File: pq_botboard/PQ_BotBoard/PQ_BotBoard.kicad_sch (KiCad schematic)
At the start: 28 parts, among them IC1 TCN75AVOA713, J1 53261-1471, J2 Conn_01x08_MountingPin, J3 53261-0271

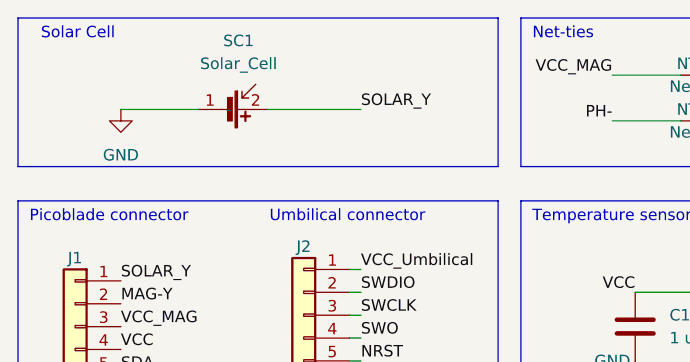
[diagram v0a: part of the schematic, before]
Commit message: Updated outer boards design as required by the change from Azur Space house-cut solar cells to Lighttricity's S3040_CIC model. Preserved the older design in lat_board_old
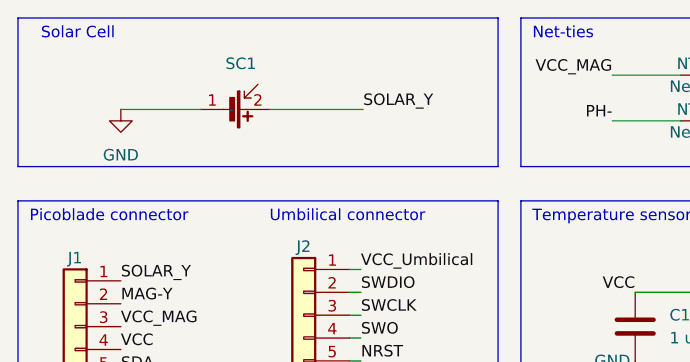
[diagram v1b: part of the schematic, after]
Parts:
- removed SC1: Solar_Cell, -nsl_power:Azur-Space-PQ-cut-SC, symbol power-nsl:Solar_Cell
- added SC1: ~, power-nsl:Lighttricity_S3040_CIC, symbol power-nsl:S3040_CIC
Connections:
- net GND: now also SC1.1 (-)
- net SOLAR_Y: now also SC1.2
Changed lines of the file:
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@@
     (stroke (width 0) (type default))
   )
-  (wire (pts (xy 87.63 52.07) (xy 96.266 52.07))
+  (wire (pts (xy 87.63 52.07) (xy 96.52 52.07))
     (stroke (width 0) (type default))
   )
@@
     (stroke (width 0) (type default))
   )
+  (wire (pts (xy 104.14 52.07) (xy 114.554 52.07))
+    (stroke (width 0) (type default))
+  )
   (wire (pts (xy 191.77 72.39) (xy 191.77 77.47))
     (stroke (width 0) (type default))
@@
   )
   (wire (pts (xy 114.3 85.09) (xy 113.03 85.09))
-    (stroke (width 0) (type default))
-  )
-  (wire (pts (xy 103.886 52.07) (xy 114.3 52.07))
     (stroke (width 0) (type default))
   )
@@
     (effects (font (size 1.27 1.27)) (justify right bottom))
   )
-  (label "SOLAR_Y" (at 114.3 52.07 0) (fields_autoplaced)
+  (label "SOLAR_Y" (at 114.554 52.07 0) (fields_autoplaced)
     (effects (font (size 1.27 1.27)) (justify left bottom))
   )
@@
         (path "/e40a5bef-c31a-474e-b379-53d1d13d8a60"
           (reference "#PWR0108") (unit 1)
+        )
+      )
+    )
+  )
+  (symbol (lib_id "power-nsl:S3040_CIC") (at 100.33 52.07 270) (unit 1)
+    (in_bom yes) (on_board yes) (dnp no) (fields_autoplaced)
+    (property "Reference" "SC1" (at 100.965 46.99 90)
+      (effects (font (size 1.27 1.27)))
+    )
+    (property "Value" "~" (at 100.33 52.07 0)
+      (effects (font (size 1.27 1.27)))
+    )
+    (property "Footprint" "power-nsl:Lighttricity_S3040_CIC" (at 100.33 52.07 0)
+      (effects (font (size 1.27 1.27)) hide)
+    )
+    (property "Datasheet" "" (at 100.33 52.07 0)
+      (effects (font (size 1.27 1.27)) hide)
+    )
+    (pin "1")
+    (pin "2")
+    (instances
+      (project "PQ_BotBoard"
+        (path "/e40a5bef-c31a-474e-b379-53d1d13d8a60"
+          (reference "SC1") (unit 1)
         )
       )
@@
         )
       )
-    )
-  )
-  (symbol (lib_id "power-nsl:Solar_Cell") (at 100.33 52.07 270) (unit 1)
-    (in_bom yes) (on_board yes) (dnp no) (fields_autoplaced)
-    (property "Reference" "SC1" (at 100.711 44.45 90)
-      (effects (font (size 1.27 1.27)))
-    )
-    (property "Value" "Solar_Cell" (at 100.711 46.99 90)
-      (effects (font (size 1.27 1.27)))
-    )
-    (property "Footprint" "-nsl_power:Azur-Space-PQ-cut-SC" (at 98.806 62.484 0)
-      (effects (font (size 1.27 1.27)) hide)
-    )
-    (property "Datasheet" "" (at 98.806 62.484 0)
-      (effects (font (size 1.27 1.27)) hide)
-    )
-    (property "Manufacturer 1" "Azur Space" (at 100.33 52.07 0)
-      (effects (font (size 1.27 1.27)) hide)
-    )
-    (property "Manufacturer Part Number 1" "3G30A" (at 100.33 52.07 0)
-      (effects (font (size 1.27 1.27)) hide)
-    )
-    (property "Supplier 1" "Lighttricity" (at 100.33 52.07 0)
-      (effects (font (size 1.27 1.27)) hide)
-    )
-    (property "Supplier Part Number 1" "N/A" (at 100.33 52.07 0)
-      (effects (font (size 1.27 1.27)) hide)
-    )
-    (pin "1")
-    (pin "2")
-    (instances
-      (project "PQ_BotBoard"
-        (path "/e40a5bef-c31a-474e-b379-53d1d13d8a60"
-          (reference "SC1") (unit 1)
-        )
-      )

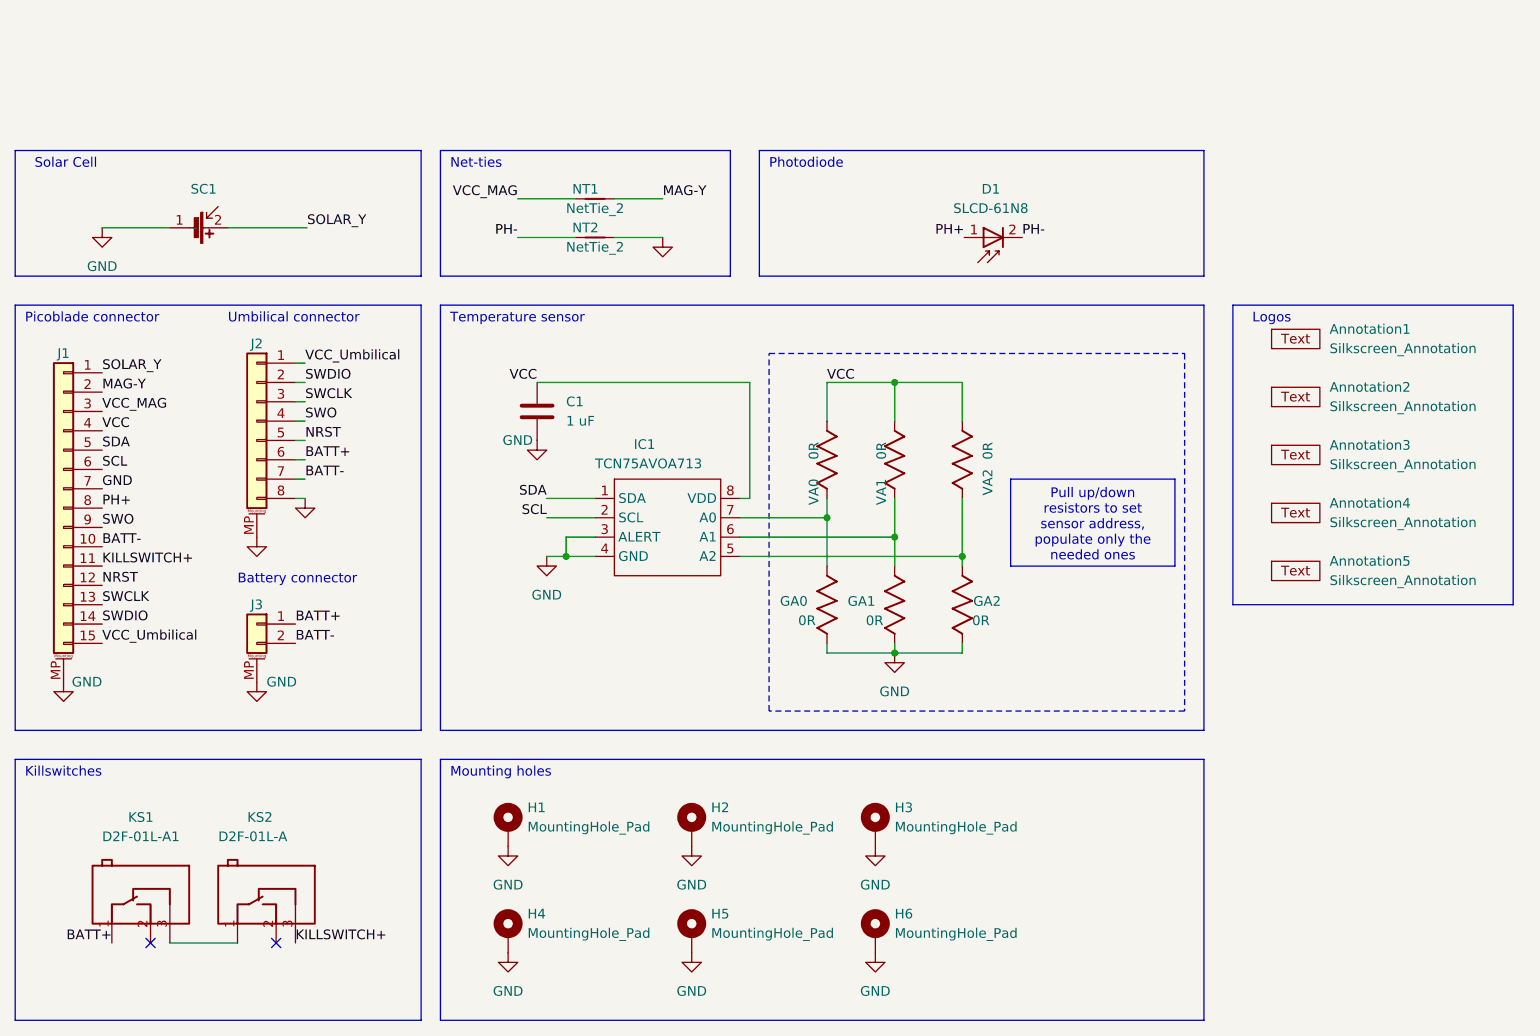
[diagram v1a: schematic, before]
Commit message: fix mirroring of Lightricity's solar cells
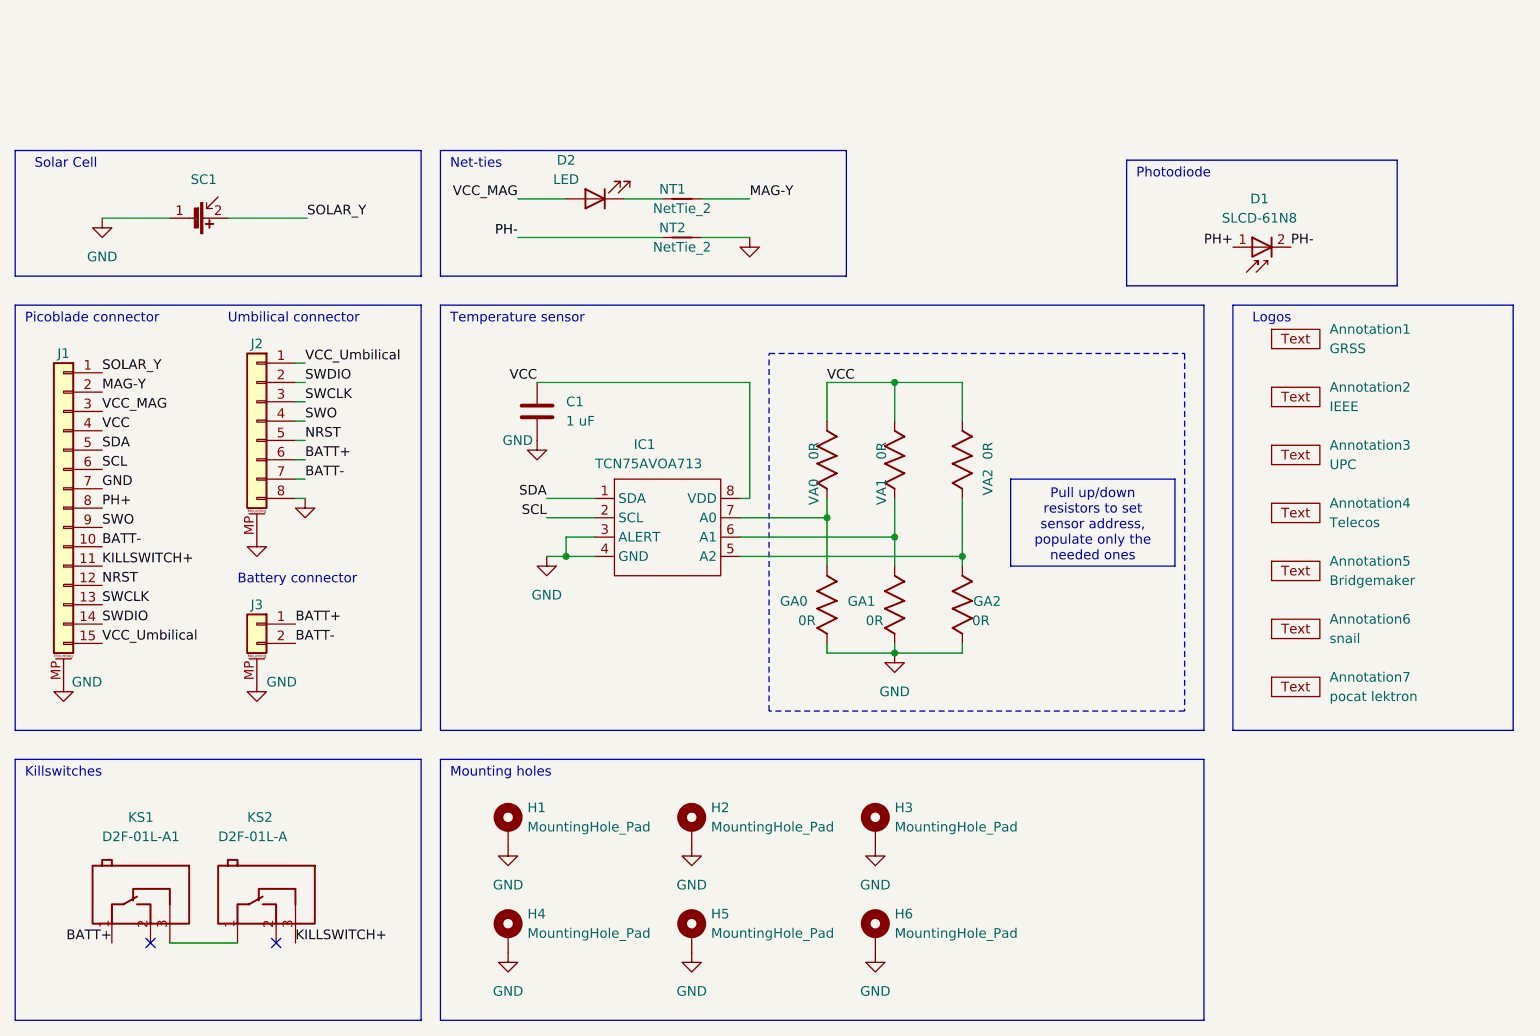
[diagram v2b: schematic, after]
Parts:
- added Annotation6: snail, symbols-nsl:snail, symbol symbols-nsl:Silkscreen_Annotation
- added Annotation7: pocat lektron, symbols-nsl:pocat-lektron, symbol symbols-nsl:Silkscreen_Annotation
- added D2: LED, LED_SMD:LED_0402_1005Metric, symbol Device:LED
- Annotation1: value Silkscreen_Annotation -> GRSS
- Annotation2: value Silkscreen_Annotation -> IEEE
- Annotation3: value Silkscreen_Annotation -> UPC
- Annotation4: value Silkscreen_Annotation -> Telecos
- Annotation5: value Silkscreen_Annotation -> Bridgemaker
- SC1: footprint power-nsl:Lighttricity_S3040_CIC -> power-nsl:Lighttricity_S3040_CIC_
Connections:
- net VCC_MAG: now also D2.2 (A); no longer NT1.1
- new net: D2.1 (K), NT1.1
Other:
- moved on the sheet: D1, NT1, NT2, SC1

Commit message: Removed netie, updated SC footprint, trace reform, logo&name cleanup, footprint reconciled, DRC, centered umbilical connector
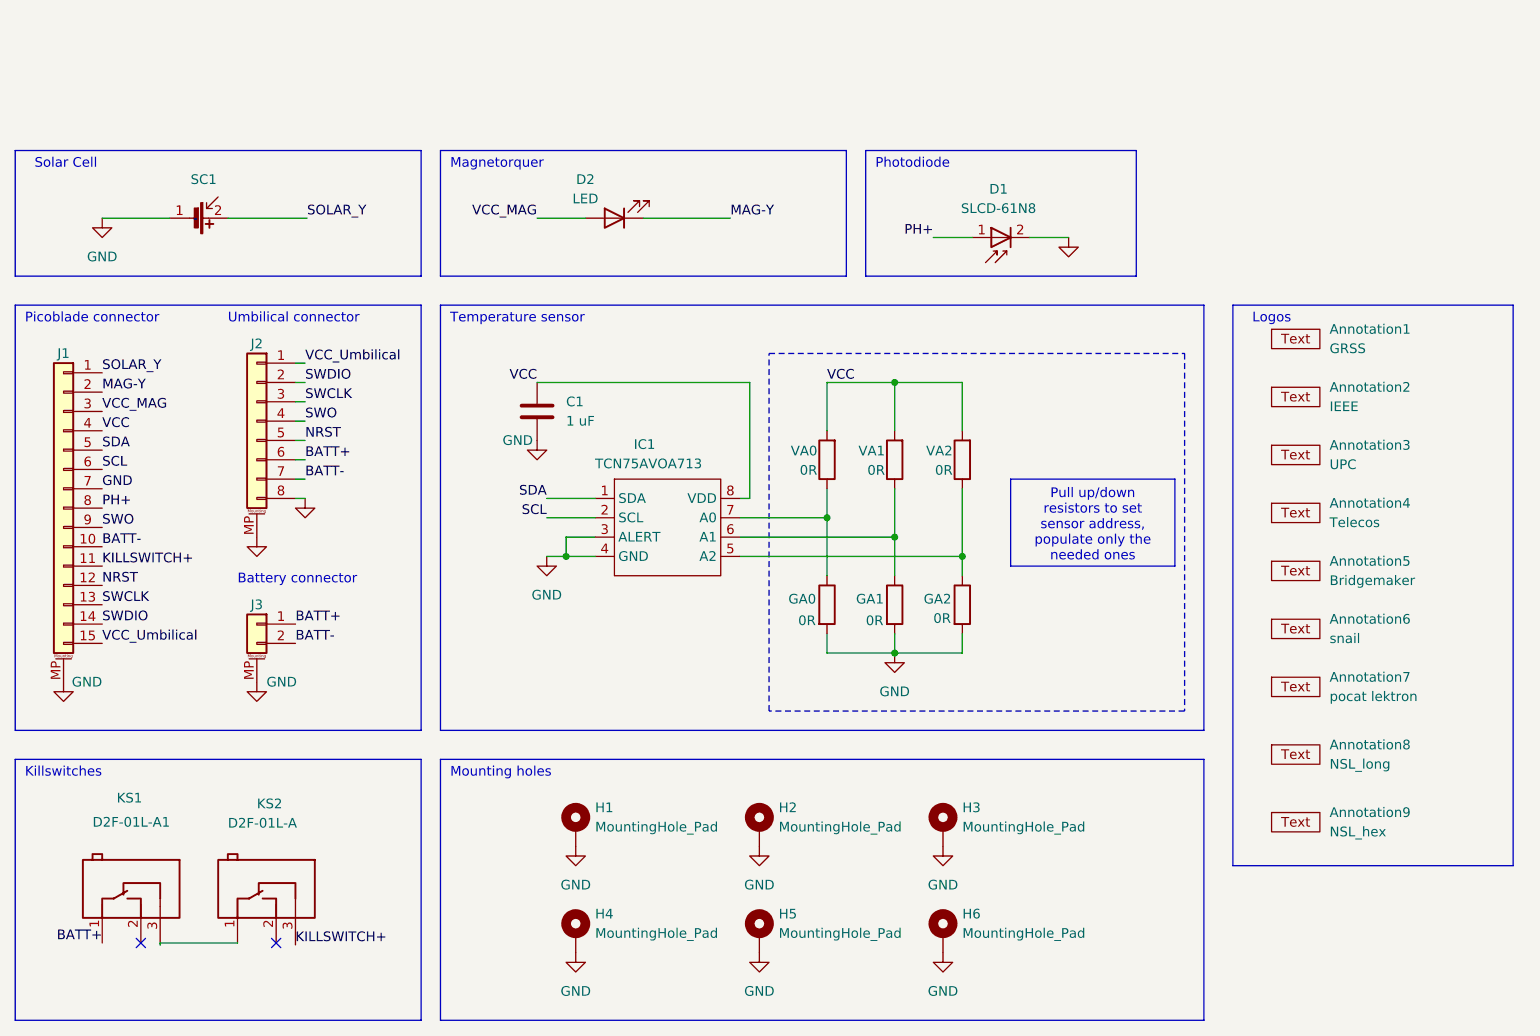
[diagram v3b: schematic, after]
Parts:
- removed NT1, NT2: NetTie_2, NetTie:NetTie-2_SMD_Pad0.5mm, symbol Device:NetTie_2
- added Annotation8: NSL_long, symbols-nsl:NSL-small, symbol symbols-nsl:Silkscreen_Annotation
- added Annotation9: NSL_hex, symbols-nsl:NSL_hexagon, symbol symbols-nsl:Silkscreen_Annotation
- Annotation1: footprint -nsl_symbols:GRSS -> symbols-nsl:GRSS
- Annotation2: footprint -nsl_symbols:IEEE_logo -> symbols-nsl:IEEE_logo
- Annotation3: footprint -nsl_symbols:UPC_positiu -> symbols-nsl:UPC_positiu
- Annotation4: footprint -nsl_symbols:Telecos -> symbols-nsl:Telecos
- Annotation5: footprint -nsl_symbols:Bridgemaker -> symbols-nsl:Bridgemaker
- Annotation6: footprint symbols-nsl:snail -> symbols-nsl:Snail
- D1: footprint -nsl_passive:SLCD-61N8 -> passive-nsl:SLCD-61N8
- GA0, GA1, GA2: symbol Lateral_board-altium-import:1_5k -> Device:R
- IC1: footprint -nsl_sensor:TCN75AVOA -> sensor-nsl:TCN75AVOA
- KS1: footprint -nsl_miscellaneous:D2FLA1 -> miscelaneous-nsl:D2FLA1; symbol Bottom_board-altium-import:0_D2F-01L-A -> miscelaneous-nsl:D2FLA
- KS2: footprint -nsl_miscellaneous:D2FLA -> miscelaneous-nsl:D2FLA; symbol Bottom_board-altium-import:0_D2F-01L-A1 -> miscelaneous-nsl:D2FLA
- SC1: footprint power-nsl:Lighttricity_S3040_CIC_ -> power-nsl:Lighttricity_S3040_CIC
- VA0, VA1, VA2: symbol Lateral_board-altium-import:0_5k -> Device:R
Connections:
- net PH- is gone; now on net GND: D1.2
- net GND: now also GA0.2, GA1.2, GA2.2; no longer GA0.1, GA1.1, GA2.1
- net MAG-Y: now also D2.1 (K)
- net at IC1.7 (A0), VA0.1: now also GA0.1; no longer GA0.2
- net at IC1.5 (A2), VA2.1: now also GA2.1; no longer GA2.2
- net at IC1.6 (A1), VA1.1: now also GA1.1; no longer GA1.2
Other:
- note added: "Magnetorquer"
- note removed: "Net-ties"
- moved on the sheet: D1, D2, H1, H2, H3, H4, H5, H6

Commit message: Added a charging protection for the battery using the umbilical (antireturn Schottky diode and LDO) and regenerated the production files
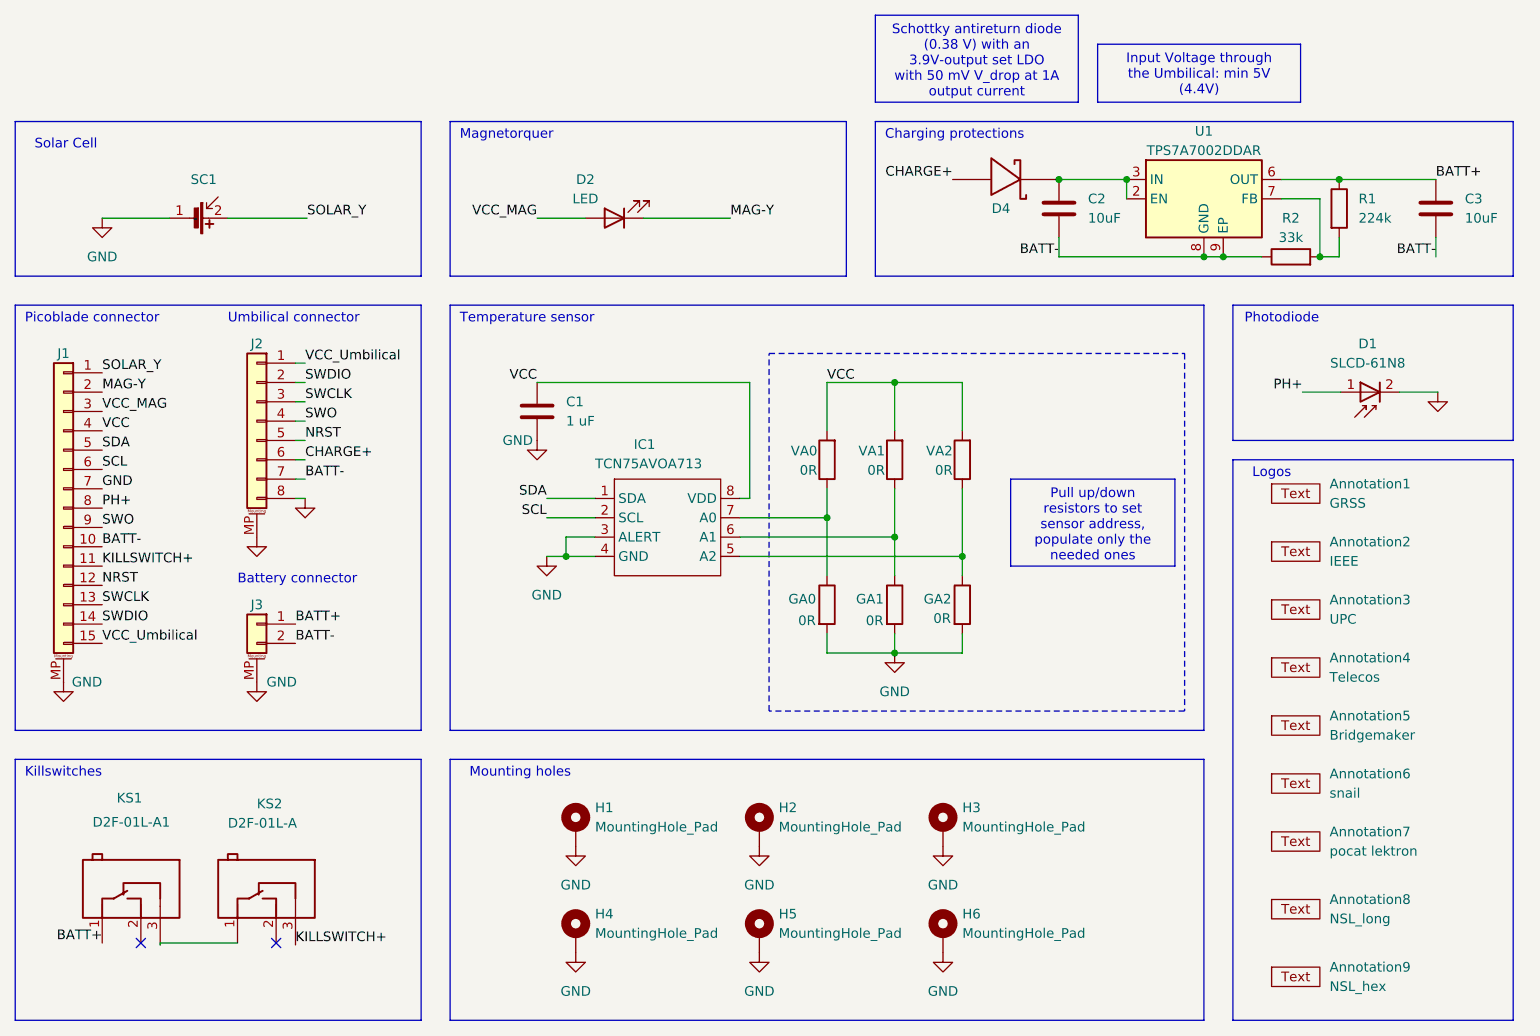
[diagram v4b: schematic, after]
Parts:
- added C2, C3: 10uF, Capacitor_SMD:C_0603_1608Metric, symbol Device:C
- added D4: ~, passive-nsl:RBS1LAM40ATR_Schottky, symbol passive-nsl:RBS1LAM40ATR_Schottky
- added R1: 224k, Resistor_SMD:R_0603_1608Metric, symbol Device:R
- added R2: 33k, Resistor_SMD:R_0603_1608Metric, symbol Device:R
- added U1: TPS7A7002DDAR, Package_SO:TI_SO-PowerPAD-8, symbol Regulator_Linear:TPS7A7001DDA
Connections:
- net BATT+: now also C3.1, R1.1, U1.6 (OUT); no longer J2.6 (Pin_6)
- net BATT-: now also C2.2, C3.2, R2.1, U1.8 (GND), U1.9 (EP)
- new net: C2.1, D4.1, U1.2 (EN), U1.3 (IN)
- new net: R1.2, R2.2, U1.7 (FB)
- new net CHARGE+: D4.2, J2.6 (Pin_6)
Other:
- note added: "Charging protections"
- moved on the sheet: Annotation1, Annotation2, Annotation3, Annotation4, Annotation5, Annotation6, Annotation7, Annotation8, Annotation9, D1
